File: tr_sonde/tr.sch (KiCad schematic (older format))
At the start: 103 parts, among them J1 SMA, J2 SMA, J3 SMA, K1 TR, K2 HV_MON, K3 VINHDR, Q1 PBSS4250X, Q2 MMBT2222A, Q3 STD2NK90ZT4, Q4 STD2NK90ZT4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

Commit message: updated component values for driver, agc, and tr switch
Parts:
- C12: value 20uF -> 22uF
- C24: value 10uF -> 22uF
- C25, C27: value 47uF -> 22uF
- C30: value 2.2uF -> .47uF
- C34: value 4700pF -> .022uF
- C8: value 20uF -> 2.2uF
- R14: value 1M -> 9.09M
- R15: value 90 OHM NTC -> 100 OHM PTC
- R16: value 20k -> 5.1k
- R17: value 20k -> 10k
- R18: value 2k -> 2k2
- R6, R7: value 43 -> 300
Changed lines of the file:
@@
 P 12150 1750
 F 0 "R15" V 12230 1700 50  0000 C CNN
-F 1 "90 OHM NTC" V 12070 1810 50  0000 C CNN
+F 1 "100 OHM PTC" V 12070 1810 50  0000 C CNN
 F 2 "smd_capacitors:c_1210" H 12150 1750 60  0001 C CNN
 F 3 "~" H 12150 1750 60  0000 C CNN
@@
 P 13250 3850
 F 0 "C24" H 13300 3950 40  0000 L CNN
-F 1 "10uF" H 13300 3750 40  0000 L CNN
+F 1 "22uF" H 13300 3750 40  0000 L CNN
 F 2 "smd_capacitors:c_1210" H 13350 3700 30  0001 C CNN
 F 3 "~" H 13250 3850 300 0000 C CNN
@@
 P 8400 2550
 F 0 "C25" H 8450 2650 40  0000 L CNN
-F 1 "47uF" H 8450 2450 40  0000 L CNN
+F 1 "22uF" H 8450 2450 40  0000 L CNN
 F 2 "smd_capacitors:c_1210" H 8500 2400 30  0001 C CNN
 F 3 "~" H 8400 2550 300 0000 C CNN
@@
 P 8750 2550
 F 0 "C27" H 8800 2650 40  0000 L CNN
-F 1 "47uF" H 8800 2450 40  0000 L CNN
+F 1 "22uF" H 8800 2450 40  0000 L CNN
 F 2 "smd_capacitors:c_1210" H 8850 2400 30  0001 C CNN
 F 3 "~" H 8750 2550 300 0000 C CNN
@@
 P 11700 2000
 F 0 "C34" H 11700 2100 40  0000 L CNN
-F 1 "4700pF" H 11706 1915 40  0000 L CNN
+F 1 ".022uF" H 11706 1915 40  0000 L CNN
 F 2 "smd_capacitors:c_1206" H 11738 1850 30  0001 C CNN
 F 3 "~" H 11700 2000 60  0000 C CNN
@@
 P 13450 8650
 F 0 "C12" H 13500 8750 40  0000 L CNN
-F 1 "20uF" H 13500 8550 40  0000 L CNN
+F 1 "22uF" H 13500 8550 40  0000 L CNN
 F 2 "Capacitors_SMD:c_1210" H 13550 8500 30  0001 C CNN
 F 3 "~" H 13450 8650 300 0000 C CNN
@@
 P 12450 8650
 F 0 "C8" H 12500 8750 40  0000 L CNN
-F 1 "20uF" H 12500 8550 40  0000 L CNN
+F 1 "2.2uF" H 12500 8550 40  0000 L CNN
 F 2 "smd_capacitors:c_0805" H 12550 8500 30  0001 C CNN
 F 3 "~" H 12450 8650 300 0000 C CNN
@@
 P 13500 2050
 F 0 "C30" H 13500 2150 40  0000 L CNN
-F 1 "2.2uF" H 13506 1965 40  0000 L CNN
+F 1 ".47uF" H 13506 1965 40  0000 L CNN
 F 2 "Capacitors_SMD:c_2225" H 13538 1900 30  0001 C CNN
 F 3 "~" H 13500 2050 60  0000 C CNN
@@
 P 9200 7900
 F 0 "R6" V 9280 7900 40  0000 C CNN
-F 1 "43" V 9207 7901 40  0000 C CNN
+F 1 "300" V 9207 7901 40  0000 C CNN
 F 2 "smd_capacitors:c_1210" V 9130 7900 30  0001 C CNN
 F 3 "~" H 9200 7900 30  0000 C CNN
@@
 P 11000 9150
 F 0 "R7" V 11080 9150 40  0000 C CNN
-F 1 "43" V 11007 9151 40  0000 C CNN
+F 1 "300" V 11007 9151 40  0000 C CNN
 F 2 "smd_capacitors:c_1210" V 10930 9150 30  0001 C CNN
 F 3 "~" H 11000 9150 30  0000 C CNN
@@
 P 15300 3300
 F 0 "R14" V 15380 3300 40  0000 C CNN
-F 1 "1M" V 15307 3301 40  0000 C CNN
+F 1 "9.09M" V 15307 3301 40  0000 C CNN
 F 2 "smd_capacitors:c_0805" V 15230 3300 30  0001 C CNN
 F 3 "~" H 15300 3300 30  0000 C CNN
@@
 P 15300 4000
 F 0 "R16" V 15380 4000 40  0000 C CNN
-F 1 "20k" V 15307 4001 40  0000 C CNN
+F 1 "5.1k" V 15307 4001 40  0000 C CNN
 F 2 "smd_capacitors:c_0805" V 15230 4000 30  0001 C CNN
 F 3 "~" H 15300 4000 30  0000 C CNN
@@
 P 15300 4650
 F 0 "R17" V 15380 4650 40  0000 C CNN
-F 1 "20k" V 15307 4651 40  0000 C CNN
+F 1 "10k" V 15307 4651 40  0000 C CNN
 F 2 "smd_capacitors:c_0805" V 15230 4650 30  0001 C CNN
 F 3 "~" H 15300 4650 30  0000 C CNN
@@
 P 16100 8150
 F 0 "R18" V 16180 8150 40  0000 C CNN
-F 1 "2k" V 16107 8151 40  0000 C CNN
+F 1 "2k2" V 16107 8151 40  0000 C CNN
 F 2 "smd_capacitors:c_0805" V 16030 8150 30  0001 C CNN
 F 3 "~" H 16100 8150 30  0000 C CNN
@@
 Wire Wire Line
 	550  7950 2400 7950
-Connection ~ 1550 8750
 Wire Wire Line
 	550  8750 2450 8750

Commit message: updated tr board to remove DNP components
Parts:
- removed C14, C16, C19, C21: DNP, smd_capacitors:c_0805, symbol C
- removed C4: 100nF, smd_capacitors:c_0805, symbol C
- removed C8: 2.2uF, smd_capacitors:c_0805, symbol CAPAPOL
- removed R10, R4, R5, R8, R9: 0, smd_capacitors:c_0805, symbol R
- removed R20, R23, R24, R26: DNP, smd_capacitors:c_0805, symbol R
- removed U4: OKI-78SR-5/1.5-W36H-C, Transistors_TO-220:TO-220_Neutral123_Horizontal_LargePads, symbol LM7805CT
- C10: value 4700pF -> 4700pF 600V
- C15, C2, C6: value .022uF -> .022uF 600 V
- C30: value .47uF -> .47uF 600V
- C33: value 4700pF -> 4700pF 600 V
- C34: value .022uF -> .022uF 600V
- C5: value 68nF -> 68nF 600V
- C9: value .022uF -> .022uF, 600 V
- D9: value SMBJ250CACT-ND -> P6SMB550CA
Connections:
- net hvd is gone; now on net hvbias: Q4.D
- net hvout is gone; now on net hvbias: C5.2, U1.6 (OUT)
- net hvs is gone; now on net hvbias: Q3.S
- net at U1.5 (LVG): now also Q4.G
- net at U1.7 (HVG): now also Q3.G
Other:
- moved on the sheet: R11

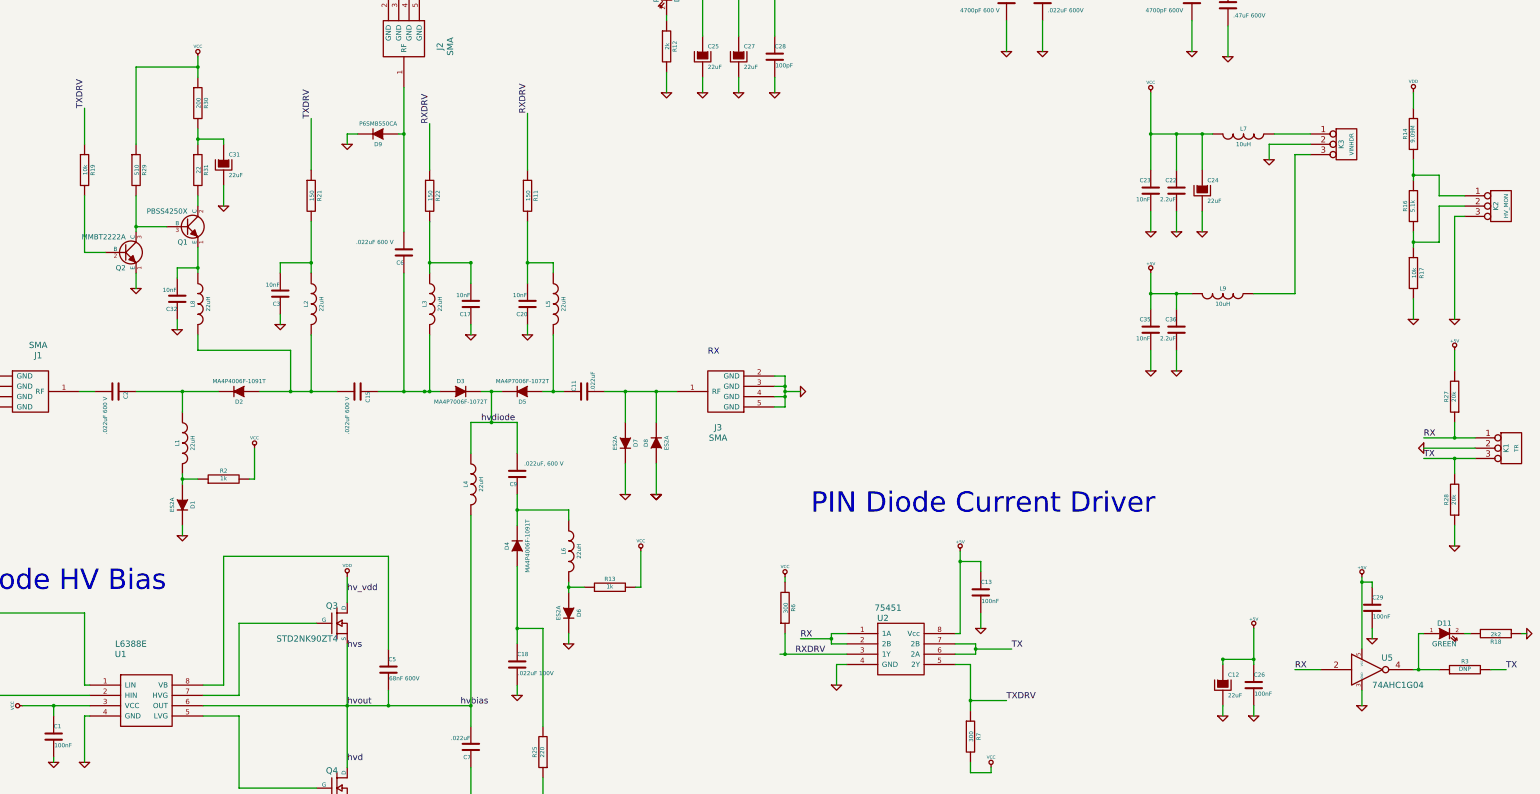
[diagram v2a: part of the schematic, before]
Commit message: picked tx hptr diode bias with higher linearity, added missing resistors for coupler in control board
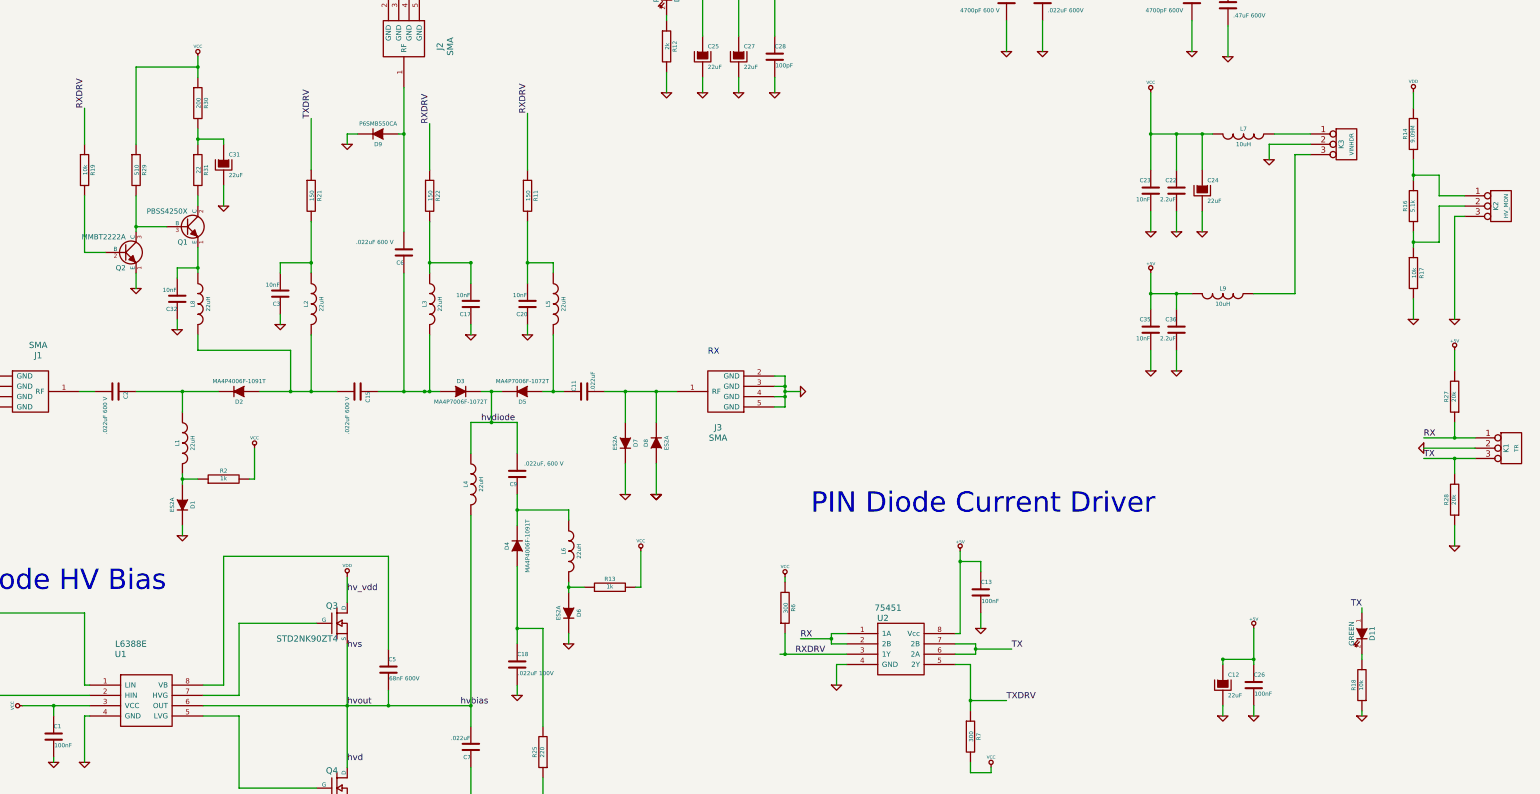
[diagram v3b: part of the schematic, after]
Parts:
- removed C29: 100nF, smd_capacitors:c_0805, symbol C
- removed R3: DNP, smd_capacitors:c_0805, symbol R
- removed U5: 74AHC1G04, SMD_Packages:SOT23-5, symbol 74AHC1G04
- R18: value 2k2 -> 10k
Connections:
- net RXDRV: now also R19.1
- net TX: now also D11.1 (A)
- net TXDRV: no longer R19.1
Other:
- moved on the sheet: D11, R18
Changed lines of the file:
@@
 	1    0    0    -1
 $EndComp
-$Comp
-L 74AHC1G04 U5
-U 1 1 537E7A3B
-P 14850 8500
-F 0 "U5" H 15045 8615 60  0000 C CNN
-F 1 "74AHC1G04" H 15150 8350 60  0000 C CNN
-F 2 "SMD_Packages:SOT23-5" H 14850 8500 60  0001 C CNN
-F 3 "" H 14850 8500 60  0000 C CNN
-	1    14850 8500
-	1    0    0    -1
-$EndComp
-$Comp
-L +5V #PWR042
-U 1 1 537E7A4D
-P 14800 7600
-F 0 "#PWR042" H 14800 7690 20  0001 C CNN
-F 1 "+5V" H 14800 7690 30  0000 C CNN
-F 2 "" H 14800 7600 60  0000 C CNN
-F 3 "" H 14800 7600 60  0000 C CNN
-	1    14800 7600
-	1    0    0    -1
-$EndComp
-$Comp
-L GND #PWR043
-U 1 1 537E7A58
-P 14800 8850
-F 0 "#PWR043" H 14800 8850 30  0001 C CNN
-F 1 "GND" H 14800 8780 30  0001 C CNN
-F 2 "" H 14800 8850 60  0000 C CNN
-F 3 "" H 14800 8850 60  0000 C CNN
-	1    14800 8850
-	1    0    0    -1
-$EndComp
-Text Label 14150 8500 0    60   ~ 0
-RX
-Text Label 16200 8500 0    60   ~ 0
+Text Label 14800 7900 2    60   ~ 0
 TX
-$Comp
-L R R3
-U 1 1 537E80D5
-P 15800 8500
-F 0 "R3" V 15880 8500 40  0000 C CNN
-F 1 "DNP" V 15807 8501 40  0000 C CNN
-F 2 "smd_capacitors:c_0805" V 15730 8500 30  0001 C CNN
-F 3 "~" H 15800 8500 30  0000 C CNN
-	1    15800 8500
-	0    -1   -1   0
-$EndComp
-$Comp
-L C C29
-U 1 1 537E830E
-P 14900 7900
-F 0 "C29" H 14900 8000 40  0000 L CNN
-F 1 "100nF" H 14906 7815 40  0000 L CNN
-F 2 "smd_capacitors:c_0805" H 14938 7750 30  0001 C CNN
-F 3 "~" H 14900 7900 60  0000 C CNN
-	1    14900 7900
-	1    0    0    -1
-$EndComp
-$Comp
-L GND #PWR044
-U 1 1 537E8438
-P 14900 8200
-F 0 "#PWR044" H 14900 8200 30  0001 C CNN
-F 1 "GND" H 14900 8130 30  0001 C CNN
-F 2 "" H 14900 8200 60  0000 C CNN
-F 3 "" H 14900 8200 60  0000 C CNN
-	1    14900 8200
-	1    0    0    -1
-$EndComp
 $Comp
 L xxSAxxxx U3
@@
 $EndComp
 $Comp
-L GND #PWR045
+L GND #PWR042
 U 1 1 537E74F6
 P 9300 1550
-F 0 "#PWR045" H 9300 1550 30  0001 C CNN
+F 0 "#PWR042" H 9300 1550 30  0001 C CNN
 F 1 "GND" H 9300 1480 30  0001 C CNN
 F 2 "" H 9300 1550 60  0000 C CNN
@@
 $EndComp
 $Comp
-L GND #PWR046
+L GND #PWR043
 U 1 1 537E78FB
 P 9100 2900
-F 0 "#PWR046" H 9100 2900 30  0001 C CNN
+F 0 "#PWR043" H 9100 2900 30  0001 C CNN
 F 1 "GND" H 9100 2830 30  0001 C CNN
 F 2 "" H 9100 2900 60  0000 C CNN
@@
 $EndComp
 $Comp
-L GND #PWR047
+L GND #PWR044
 U 1 1 537E7FEF
 P 10950 1550
-F 0 "#PWR047" H 10950 1550 30  0001 C CNN
+F 0 "#PWR044" H 10950 1550 30  0001 C CNN
 F 1 "GND" H 10950 1480 30  0001 C CNN
 F 2 "" H 10950 1550 60  0000 C CNN
@@
 $EndComp
 $Comp
-L GND #PWR048
+L GND #PWR045
 U 1 1 537E9221
 P 13500 2550
-F 0 "#PWR048" H 13500 2550 30  0001 C CNN
+F 0 "#PWR045" H 13500 2550 30  0001 C CNN
 F 1 "GND" H 13500 2480 30  0001 C CNN
 F 2 "" H 13500 2550 60  0000 C CNN
@@
 $EndComp
 $Comp
-L VCC #PWR049
+L VCC #PWR046
 U 1 1 537F9103
 P 9200 7600
-F 0 "#PWR049" H 9200 7700 30  0001 C CNN
+F 0 "#PWR046" H 9200 7700 30  0001 C CNN
 F 1 "VCC" H 9200 7700 30  0000 C CNN
 F 2 "" H 9200 7600 60  0000 C CNN
@@
 $EndComp
 $Comp
-L VCC #PWR050
+L VCC #PWR047
 U 1 1 537F913B
 P 11200 9450
-F 0 "#PWR050" H 11200 9550 30  0001 C CNN
+F 0 "#PWR047" H 11200 9550 30  0001 C CNN
 F 1 "VCC" H 11200 9550 30  0000 C CNN
 F 2 "" H 11200 9450 60  0000 C CNN
@@
 $EndComp
 $Comp
-L VDD #PWR051
+L VDD #PWR048
 U 1 1 537FA30C
 P 15300 2900
-F 0 "#PWR051" H 15300 3000 30  0001 C CNN
+F 0 "#PWR048" H 15300 3000 30  0001 C CNN
 F 1 "VDD" H 15300 3010 30  0000 C CNN
 F 2 "" H 15300 2900 60  0000 C CNN
@@
 $EndComp
 $Comp
-L GND #PWR052
+L GND #PWR049
 U 1 1 537FA865
 P 15300 5100
-F 0 "#PWR052" H 15300 5100 30  0001 C CNN
+F 0 "#PWR049" H 15300 5100 30  0001 C CNN
 F 1 "GND" H 15300 5030 30  0001 C CNN
 F 2 "" H 15300 5100 60  0000 C CNN
@@
 $EndComp
 $Comp
-L GND #PWR053
+L GND #PWR050
 U 1 1 537FAD00
 P 15700 5100
-F 0 "#PWR053" H 15700 5100 30  0001 C CNN
+F 0 "#PWR050" H 15700 5100 30  0001 C CNN
 F 1 "GND" H 15700 5030 30  0001 C CNN
 F 2 "" H 15700 5100 60  0000 C CNN
@@
 $EndComp
 $Comp
-L VCC #PWR054
+L VCC #PWR051
 U 1 1 537FAE62
 P 8050 1400
-F 0 "#PWR054" H 8050 1500 30  0001 C CNN
+F 0 "#PWR051" H 8050 1500 30  0001 C CNN
 F 1 "VCC" H 8050 1500 30  0000 C CNN
 F 2 "" H 8050 1400 60  0000 C CNN
@@
 $EndComp
 $Comp
-L GND #PWR055
+L GND #PWR052
 U 1 1 537FB0A2
 P 8050 2900
-F 0 "#PWR055" H 8050 2900 30  0001 C CNN
+F 0 "#PWR052" H 8050 2900 30  0001 C CNN
 F 1 "GND" H 8050 2830 30  0001 C CNN
 F 2 "" H 8050 2900 60  0000 C CNN
@@
 L LED D11
 U 1 1 537FB409
-P 15600 8150
-F 0 "D11" H 15600 8250 50  0000 C CNN
-F 1 "GREEN" H 15600 8050 50  0000 C CNN
-F 2 "LEDs:LED-0805" H 15600 8150 60  0001 C CNN
-F 3 "" H 15600 8150 60  0000 C CNN
-	1    15600 8150
-	1    0    0    -1
+P 14800 8150
+F 0 "D11" H 14800 8250 50  0000 C CNN
+F 1 "GREEN" H 14800 8050 50  0000 C CNN
+F 2 "LEDs:LED-0805" H 14800 8150 60  0001 C CNN
+F 3 "" H 14800 8150 60  0000 C CNN
+	1    14800 8150
+	0    1    1    0
 $EndComp
 $Comp
 L R R18
 U 1 1 537FB40F
-P 16100 8150
-F 0 "R18" V 16180 8150 40  0000 C CNN
-F 1 "2k2" V 16107 8151 40  0000 C CNN
-F 2 "smd_capacitors:c_0805" V 16030 8150 30  0001 C CNN
-F 3 "~" H 16100 8150 30  0000 C CNN
-	1    16100 8150
-	0    1    1    0
-$EndComp
-$Comp
-L GND #PWR056
+P 14800 8650
+F 0 "R18" V 14880 8650 40  0000 C CNN
+F 1 "10k" V 14807 8651 40  0000 C CNN
+F 2 "smd_capacitors:c_0805" V 14730 8650 30  0001 C CNN
+F 3 "~" H 14800 8650 30  0000 C CNN
+	1    14800 8650
+	-1   0    0    1
+$EndComp
+$Comp
+L GND #PWR053
 U 1 1 537FB41D
-P 16400 8150
-F 0 "#PWR056" H 16400 8150 30  0001 C CNN
-F 1 "GND" H 16400 8080 30  0001 C CNN
-F 2 "" H 16400 8150 60  0000 C CNN
-F 3 "" H 16400 8150 60  0000 C CNN
-	1    16400 8150
-	0    -1   -1   0
-$EndComp
-$Comp
-L GND #PWR057
+P 14800 8950
+F 0 "#PWR053" H 14800 8950 30  0001 C CNN
+F 1 "GND" H 14800 8880 30  0001 C CNN
+F 2 "" H 14800 8950 60  0000 C CNN
+F 3 "" H 14800 8950 60  0000 C CNN
+	1    14800 8950
+	1    0    0    -1
+$EndComp
+$Comp
+L GND #PWR054
 U 1 1 537FBBB2
 P 2900 4800
-F 0 "#PWR057" H 2900 4800 30  0001 C CNN
+F 0 "#PWR054" H 2900 4800 30  0001 C CNN
 F 1 "GND" H 2900 4730 30  0001 C CNN
 F 2 "" H 2900 4800 60  0000 C CNN
@@
 $EndComp
 $Comp
-L VCC #PWR058
+L VCC #PWR055
 U 1 1 537FC621
 P 3500 2550
-F 0 "#PWR058" H 3500 2650 30  0001 C CNN
+F 0 "#PWR055" H 3500 2650 30  0001 C CNN
 F 1 "VCC" H 3500 2650 30  0000 C CNN
 F 2 "" H 3500 2550 60  0000 C CNN
@@
 $EndComp
 $Comp
-L GND #PWR059
+L GND #PWR056
 U 1 1 537FC782
 P 3750 4000
-F 0 "#PWR059" H 3750 4000 30  0001 C CNN
+F 0 "#PWR056" H 3750 4000 30  0001 C CNN
 F 1 "GND" H 3750 3930 30  0001 C CNN
 F 2 "" H 3750 4000 60  0000 C CNN
@@
 $EndComp
 Text Label 2400 3050 1    60   ~ 0
-TXDRV
+RXDRV
 $Comp
 L NPN Q2
@@
 $EndComp
 $Comp
-L GND #PWR060
+L GND #PWR057
 U 1 1 537FD975
 P 3300 5200
-F 0 "#PWR060" H 3300 5200 30  0001 C CNN
+F 0 "#PWR057" H 3300 5200 30  0001 C CNN
 F 1 "GND" H 3300 5130 30  0001 C CNN
 F 2 "" H 3300 5200 60  0000 C CNN
@@
 $EndComp
 $Comp
-L +5V #PWR061
+L +5V #PWR058
 U 1 1 5384E6DA
 P 8400 1350
-F 0 "#PWR061" H 8400 1440 20  0001 C CNN
+F 0 "#PWR058" H 8400 1440 20  0001 C CNN
 F 1 "+5V" H 8400 1440 30  0000 C CNN
 F 2 "" H 8400 1350 60  0000 C CNN
@@
 $EndComp
 $Comp
-L +5V #PWR062
+L +5V #PWR059
 U 1 1 5384E820
 P 12750 4650
-F 0 "#PWR062" H 12750 4740 20  0001 C CNN
+F 0 "#PWR059" H 12750 4740 20  0001 C CNN
 F 1 "+5V" H 12750 4740 30  0000 C CNN
 F 2 "" H 12750 4650 60  0000 C CNN
@@
 $EndComp
 $Comp
-L GND #PWR063
+L GND #PWR060
 U 1 1 5384F0ED
 P 13000 5600
-F 0 "#PWR063" H 13000 5600 30  0001 C CNN
+F 0 "#PWR060" H 13000 5600 30  0001 C CNN
 F 1 "GND" H 13000 5530 30  0001 C CNN
 F 2 "" H 13000 5600 60  0000 C CNN
@@
 $EndComp
 $Comp
-L GND #PWR064
+L GND #PWR061
 U 1 1 5384F0F3
 P 12750 5600
-F 0 "#PWR064" H 12750 5600 30  0001 C CNN
+F 0 "#PWR061" H 12750 5600 30  0001 C CNN
 F 1 "GND" H 12750 5530 30  0001 C CNN
 F 2 "" H 12750 5600 60  0000 C CNN
@@
 	3750 3800 3750 4000
 Wire Wire Line
-	16350 8150 16400 8150
-Wire Wire Line
-	15800 8150 15850 8150
-Connection ~ 15350 8500
-Wire Wire Line
-	15350 8150 15350 8500
-Wire Wire Line
-	15400 8150 15350 8150
+	14800 8900 14800 8950
+Wire Wire Line
+	14800 8350 14800 8400
+Wire Wire Line
+	14800 7950 14800 7900
 Wire Wire Line
 	8050 2700 8050 2900
@@
 Wire Wire Line
 	9300 1550 9600 1550
-Connection ~ 14800 7650
-Wire Wire Line
-	14900 7650 14900 7700
-Wire Wire Line
-	14800 7650 14900 7650
-Wire Wire Line
-	14900 8100 14900 8200
-Wire Wire Line
-	16200 8500 16050 8500
-Wire Wire Line
-	15300 8500 15550 8500
-Wire Wire Line
-	14150 8500 14400 8500
-Wire Wire Line
-	14800 8700 14800 8850
-Wire Wire Line
-	14800 7600 14800 8300
 Connection ~ 13450 8400
 Wire Wire Line
